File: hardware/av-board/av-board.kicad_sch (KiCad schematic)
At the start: 215 parts, among them J1 RCA Y, J10 2x20 socket, J2 RCA Pb, J3 RCA Pr, J4 RCA L, J5 RCA R, J6 HDMI-001, J9 2x20 socket, SW1 TS-1187A-B-A-B, SW2 TS-1187A-B-A-B, U1 ADV7842KBCZ-5, U10 TPD4E05U06DQAR, U2 ADV7511KSTZ, U3 PCM1808PWR, U4 TLV62569DBVR, U5 TPS7A7001DDAR, U6 TPS7A7001DDAR, U7 TPS7A7001DDAR, U8 TPD4E05U06DQAR, U9 TPD4E05U06DQAR, Y1 28.63636MHz 20pF

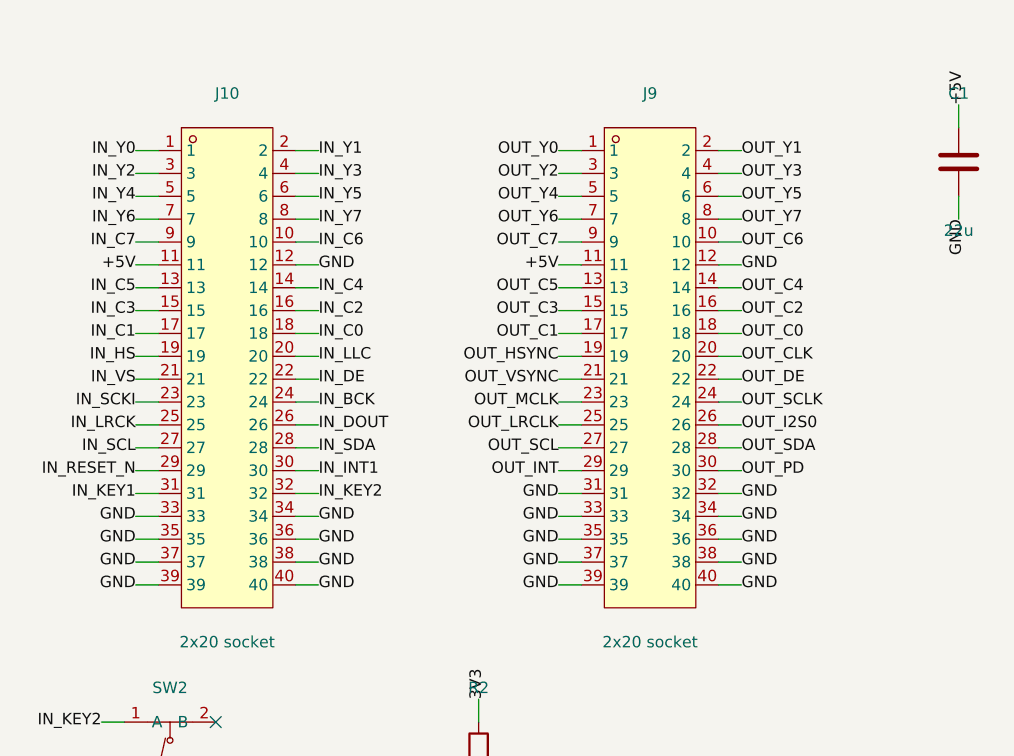
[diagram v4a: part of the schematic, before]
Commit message: Placement: parts by the pins they serve, both header buses flat
The router was failing on placement, not on routing time:

- Small parts were anchored on the first earlier IC sharing any net. Pull-ups to 3V3 went to
  the 3V3 regulator (R20-R25 near J9, 35-45 mm from their ADV7842 balls), and the 51 R
  video terminations (on TERM_x only, no IC pad) fell back to the middle of the bottom edge.
  Now a part on a signal goes to the IC pin it serves, else beside the part it hangs on, else
  the connector pin; supply nets do not count. The terminations sit at the ADV7842 (UG-214
  App. A), the ADV7511 audio series resistors at the source, J9 (HWG 7.3). Parts wait until
  what they hang on is placed.
- J10 had Y0-Y7 on its left pins while the 75 R arrays put out C0..C7 first: every line crossed
  every other in the 5 mm under the arrays. J10 is now in array order (LLC stays on the CLK
  pin: 2 crossings). J9 is in the ADV7511 pin order round the chip (0 crossings); its CLK is
  an output and leaves the header CLK pin. gen_pcb.py prints the crossings per bus.
- The PCM1808 I2S moves from J10 pins 23-26 (45 mm away) to J9 pins 37-40 (10 mm).
- The regulators move out of the band between J9 and the ADV7511 to the empty corner under it.

placecheck.py lists parts far from their nets; snap.py renders a board to PNG. design.md
pin tables follow. ERC clean, schematic = board.py on 897 pins.

Co-Authored-By: Claude Opus 5.5 <noreply@anthropic.com>
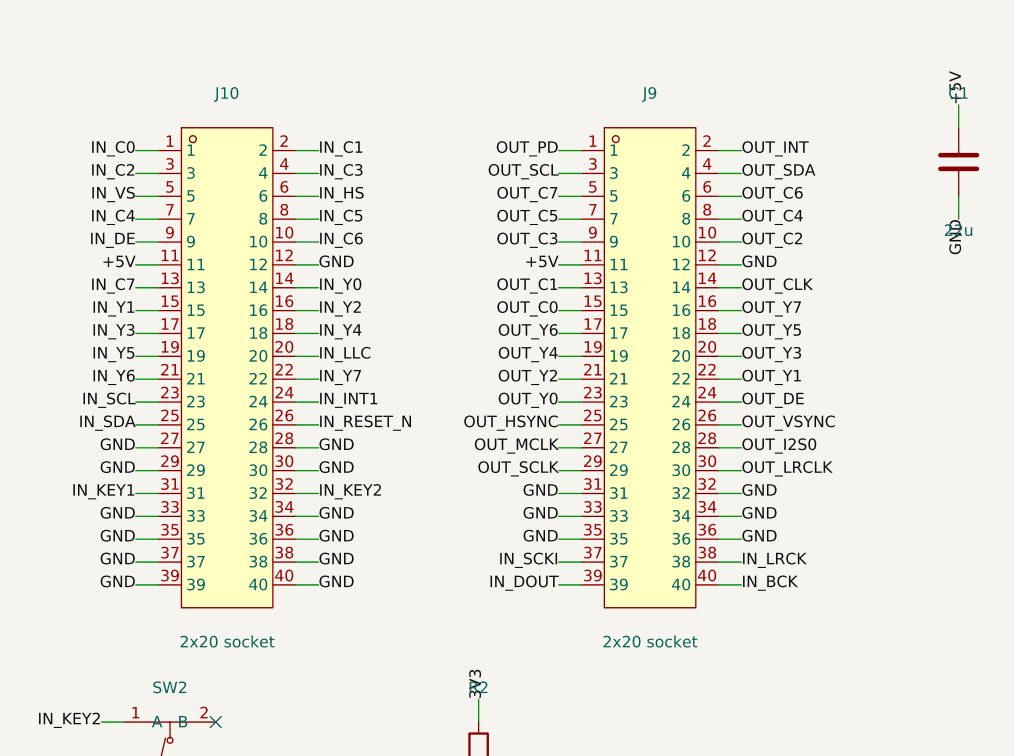
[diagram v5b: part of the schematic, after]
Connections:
- net GND: now also J10.27, J10.28, J10.29, J10.30; no longer J9.37, J9.38, J9.39, J9.40
- net IN_BCK: now also J9.40; no longer J10.24
- net IN_C0: now also J10.1; no longer J10.18
- net IN_C1: now also J10.2; no longer J10.17
- net IN_C2: now also J10.3; no longer J10.16
- net IN_C3: now also J10.4; no longer J10.15
- net IN_C4: now also J10.7; no longer J10.14
- net IN_C5: now also J10.8; no longer J10.13
- net IN_C7: now also J10.13; no longer J10.9
- net IN_DE: now also J10.9; no longer J10.22
- net IN_DOUT: now also J9.39; no longer J10.26
- net IN_HS: now also J10.6; no longer J10.19
- net IN_INT1: now also J10.24; no longer J10.30
- net IN_LRCK: now also J9.38; no longer J10.25
- net IN_RESET_N: now also J10.26; no longer J10.29
- net IN_SCKI: now also J9.37; no longer J10.23
- net IN_SCL: now also J10.23; no longer J10.27
- net IN_SDA: now also J10.25; no longer J10.28
- net IN_VS: now also J10.5; no longer J10.21
- net IN_Y0: now also J10.14; no longer J10.1
- net IN_Y1: now also J10.15; no longer J10.2
- net IN_Y2: now also J10.16; no longer J10.3
- net IN_Y3: now also J10.17; no longer J10.4
- net IN_Y4: now also J10.18; no longer J10.5
- net IN_Y5: now also J10.19; no longer J10.6
- net IN_Y6: now also J10.21; no longer J10.7
- net IN_Y7: now also J10.22; no longer J10.8
- net OUT_C0: now also J9.15; no longer J9.18
- net OUT_C1: now also J9.13; no longer J9.17
- net OUT_C2: now also J9.10; no longer J9.16
- net OUT_C3: now also J9.9; no longer J9.15
- net OUT_C4: now also J9.8; no longer J9.14
- net OUT_C5: now also J9.7; no longer J9.13
- net OUT_C6: now also J9.6; no longer J9.10
- net OUT_C7: now also J9.5; no longer J9.9
- net OUT_CLK: now also J9.14; no longer J9.20
- net OUT_DE: now also J9.24; no longer J9.22
- net OUT_HSYNC: now also J9.25; no longer J9.19
- net OUT_I2S0: now also J9.28; no longer J9.26
- net OUT_INT: now also J9.2; no longer J9.29
- net OUT_LRCLK: now also J9.30; no longer J9.25
- net OUT_MCLK: now also J9.27; no longer J9.23
- net OUT_PD: now also J9.1; no longer J9.30
- net OUT_SCL: now also J9.3; no longer J9.27
- net OUT_SCLK: now also J9.29; no longer J9.24
- net OUT_SDA: now also J9.4; no longer J9.28
- net OUT_VSYNC: now also J9.26; no longer J9.21
- net OUT_Y0: now also J9.23; no longer J9.1
- net OUT_Y1: now also J9.22; no longer J9.2
- net OUT_Y2: now also J9.21; no longer J9.3
- net OUT_Y3: now also J9.20; no longer J9.4
- net OUT_Y4: now also J9.19; no longer J9.5
- net OUT_Y5: now also J9.18; no longer J9.6
- net OUT_Y6: now also J9.17; no longer J9.7
- net OUT_Y7: now also J9.16; no longer J9.8

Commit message: Rail planes sized for their caps: 68 of 69 ADV7842 rail caps over their plane
40 of the ADV7842 rail caps sat off their planes (median 7 mm, up to 12 mm from their rail),
among them 10 per-ball 10/100 nF caps and AVDD/PVDD caps: noise on the ADC and PLL supplies,
and one more routed connection each into the crowd round the BGA.

- The planes widen past the BGA to hold their filter and every cap: AVDD over the top right,
  PVDD over the top left (taking room TVDD did not use), VDD and DVDDIO to the right with
  DVDDIO (25 caps per UG-214 Fig. 179) taking the larger lower part, up to the regulators.
- CVDD's filter and tantalum move from the right of the BGA, where they took VDD/DVDDIO room,
  to its left, four rows from the CVDD balls (C12-E12), in TVDD's spare room.
- The regulators move right, off the planes; U5/U4 spread so the buck has room.
- 10 uF rail caps go by their filter with the 33 uF ones (they are bulk), not round-robin on
  the balls under the BGA's edge.
- Bias resistors (RTERM, R_EXT), the REFP/REFN caps and the regulators' feedback dividers are
  placed before the decoupling, at their pins; the crystal moves 3 mm left, off E15/E16.
- The SDRAM pull-down arrays lose their first-place rank (meant for the 75 R arrays), so the
  analog input caps get the BGA's top edge.
- The PCM1808 VCC ferrite is written down with the PCM1808, so it sits there (was 65 mm away).

PCB=path makes a trial board elsewhere. ERC clean, schematic = board.py (897 pins), DRC: only
the unrouted connections.

Co-Authored-By: Claude Opus 5.5 <noreply@anthropic.com>
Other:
- moved on the sheet: C101, C102, C103, C104, C105, C106, C107, C108, C109, C110, FB1, J4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

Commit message: Review against the data sheets: LDO feed-forward and EN, HPD, anti-alias, clock clearance
Every IC checked pin by pin against its document (design.md "Review against the data sheets"):
the ADV7842 against every row of UG-214 App. C and the AIN_SEL routing, the ADV7511 against
HWG Rev D, the PCM1808, TPS7A7001, TLV62569 and TPD4E05U06 against their data sheets. Fixed:

- TPS7A7001: a 220 pF feed-forward across R1 on all three; the data sheet requires it with
  47-200 uF on the output (3V3 and both 1.8 V rails carry more than 47 uF through the filters).
  U6/U7 output 22 uF -> 10 uF, keeping 1V8A (about 185 uF) under the 200 uF limit.
- TPS7A7001 EN: the 1.8 V LDOs' enable RC now pulls up to 2V5, their VIN; from 3V3 it put EN
  above VIN (recommended: EN <= VIN). The 1.8 V rails still come up about 30 ms after 2V5.
- ADV7511 HPD: 10 k to GND as HWG 6.1.4 asks (was 100 k).
- PCM1808 anti-alias cap 220 pF (145 kHz, TI's range); the 1 nF cut 1.4 dB at 20 kHz.
- A CLOCK netclass (OUT_CLK, LLC) with 0.19 mm clearance, what the 0.5 mm-pitch pads allow
  (HWG 7.2: nothing near the CLK trace).

ERC clean, schematic = board.py (903 pins), DRC: only the unrouted connections.

Co-Authored-By: Claude Opus 5.5 <noreply@anthropic.com>
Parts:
- added C123, C124, C125: 100n, Capacitor_SMD:C_0402_1005Metric, symbol Device:C
- C10: value 10u -> 470n; footprint Capacitor_SMD:C_0805_2012Metric -> Capacitor_SMD:C_0603_1608Metric; LCSC C15850 -> C1623
- C100, C101, C112: value 100n -> 220p; LCSC C1525 -> C1530
- C102: value 10u -> 10n; footprint Capacitor_SMD:C_0603_1608Metric -> Capacitor_SMD:C_0402_1005Metric; LCSC C19702 -> C15195
- C104, C106: value 10u -> 100n; footprint Capacitor_SMD:C_0603_1608Metric -> Capacitor_SMD:C_0402_1005Metric; LCSC C19702 -> C1525
- C105, C29, C30, C31, C40: value 100n -> 10u; footprint Capacitor_SMD:C_0402_1005Metric -> Capacitor_SMD:C_0603_1608Metric; LCSC C1525 -> C19702
- C107, C109: value 1n -> 10u; footprint Capacitor_SMD:C_0402_1005Metric -> Capacitor_SMD:C_0603_1608Metric; LCSC C1523 -> C19702
- C108: value 1u -> 100n; footprint Capacitor_SMD:C_0603_1608Metric -> Capacitor_SMD:C_0402_1005Metric; LCSC C15849 -> C1525
- C11: value 22u -> 10u; LCSC C45783 -> C15850
- C110: value 1u -> 220p; footprint Capacitor_SMD:C_0603_1608Metric -> Capacitor_SMD:C_0402_1005Metric; LCSC C15849 -> C1530
- C111, C113: value 100n -> 1u; footprint Capacitor_SMD:C_0402_1005Metric -> Capacitor_SMD:C_0603_1608Metric; LCSC C1525 -> C15849
- C13: value 22u -> 220p; footprint Capacitor_SMD:C_0805_2012Metric -> Capacitor_SMD:C_0402_1005Metric; LCSC C45783 -> C1530
- C14: value 33u -> 10u; footprint lcsc:CAP-SMD_L3.5-W2.8-R-RD -> Capacitor_SMD:C_0805_2012Metric; symbol lcsc:TAJB336K010RNJ -> Device:C; LCSC C7202 -> C15850
- C15: footprint Capacitor_SMD:C_0603_1608Metric -> Capacitor_SMD:C_0805_2012Metric; LCSC C19702 -> C15850
- C16: value 33u -> 220p; footprint lcsc:CAP-SMD_L3.5-W2.8-R-RD -> Capacitor_SMD:C_0402_1005Metric; symbol lcsc:TAJB336K010RNJ -> Device:C; LCSC C7202 -> C1530
- C17, C19, C21, C23, C25, C27: value 10u -> 33u; footprint Capacitor_SMD:C_0603_1608Metric -> lcsc:CAP-SMD_L3.5-W2.8-R-RD; symbol Device:C -> lcsc:TAJB336K010RNJ; LCSC C19702 -> C7202
- C18, C20, C22, C24: value 33u -> 10u; footprint lcsc:CAP-SMD_L3.5-W2.8-R-RD -> Capacitor_SMD:C_0603_1608Metric; symbol lcsc:TAJB336K010RNJ -> Device:C; LCSC C7202 -> C19702
- C32: value 1n -> 100n; LCSC C1523 -> C1525
- C33, C34: value 30p -> 100n; LCSC C1570 -> C1525
- C35: value 100n -> 1n; LCSC C1525 -> C1523
- C36: value 100n -> 30p; LCSC C1525 -> C1570
- C37: value 10u -> 30p; footprint Capacitor_SMD:C_0603_1608Metric -> Capacitor_SMD:C_0402_1005Metric; LCSC C19702 -> C1570
- C38, C39, C71: value 10n -> 100n; LCSC C15195 -> C1525
- C41, C68: value 100n -> 10n; LCSC C1525 -> C15195
- C42, C56, C57, C58, C74, C75, C86, C87, C88: value 220p -> 10n; LCSC C1530 -> C15195
- C43, C44: value 220p -> 100n; LCSC C1530 -> C1525
- C51, C52, C53, C65, C66, C67, C77, C78, C99: value 10n -> 220p; LCSC C15195 -> C1530
- C6: value 4.7u -> 220p; footprint Capacitor_SMD:C_0805_2012Metric -> Capacitor_SMD:C_0402_1005Metric; LCSC C1779 -> C1530
- C7: value 10u -> 4.7u; LCSC C15850 -> C1779
- C8: value 6.8p -> 10u; footprint Capacitor_SMD:C_0402_1005Metric -> Capacitor_SMD:C_0805_2012Metric; LCSC C1576 -> C15850
- C9: value 470n -> 6.8p; footprint Capacitor_SMD:C_0603_1608Metric -> Capacitor_SMD:C_0402_1005Metric; LCSC C1623 -> C1576
- R51: value 100k -> 10k; LCSC C25741 -> C25744; Note keeps HPD low with no cable (not in HWG Fig. 27) -> 0 V on HPD with no sink [HWG 6.1.4: 10 k +-10 %]
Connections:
- net +5V: now also C7.1; no longer C6.1
- net 1V8A: now also C12.1, C13.1; no longer C11.1
- net 1V8B: now also C15.1, C16.1; no longer C13.1
- net 2V5: now also C11.1, C14.1, C9.1, R7.1; no longer C10.1, C12.1, C7.1
- net 3V3: now also C108.1, C109.1, C6.1, C124.1; no longer C105.1, C106.1, C121.1, R7.1
- net 5VA: now also C106.1, C107.1; no longer C103.1, C104.1
- net AIN_PB: now also C33.2; no longer C30.2
- net AIN_PR: now also C34.2; no longer C31.2
- net AIN_Y: now also C32.2; no longer C29.2
- net AUD_DIV_L: now also C110.1, C111.1; no longer C107.1, C108.1
- net AUD_DIV_R: now also C112.1, C113.1; no longer C109.1, C110.1
- net AUD_VINL: now also C111.2; no longer C108.2
- net AUD_VINR: now also C113.2; no longer C110.2
- net AV_AVDD: now also C19.1, C20.1, C65.1, C66.1, C67.1; no longer C16.1, C17.1, C51.1, C52.1, C53.1
- net AV_CVDD: now also C21.1, C22.1, C69.1, C70.1, C71.1; no longer C18.1, C19.1, C65.1, C66.1, C67.1
- net AV_DVDDIO: now also C100.1, C101.1, C25.1, C26.1, C99.1; no longer C22.1, C23.1, C76.1, C77.1, C78.1
- net AV_PVDD: now also C102.1, C103.1, C23.1, C24.1; no longer C100.1, C20.1, C21.1, C99.1
- net AV_TVDD: now also C27.1, C28.1, C51.1, C52.1, C53.1; no longer C24.1, C25.1, C38.1, C39.1, C40.1
- net AV_VDD: now also C17.1, C18.1, C76.1, C77.1, C78.1; no longer C14.1, C15.1, C69.1, C70.1, C71.1
- net EN_1V8: now also C10.1; no longer C9.1
- net FB_1V8A: now also C13.2
- net FB_1V8B: now also C16.2
- net FB_2V5: now also C9.2; no longer C8.2
- net FB_3V3: now also C6.2
- net GND: now also C108.2, C110.2, C29.2, C30.2, C31.2, C37.2, C8.2, C123.2, C124.2, C125.2; no longer C111.2, C113.2, C13.2, C16.2, C33.2, C34.2, C35.2, C40.2, C6.2, C9.2
- net HDMI_5V: now also C125.1; no longer C122.1
- net REFN: now also C39.1, C40.2; no longer C36.1, C37.2
- net REFP: now also C38.1, C40.1; no longer C35.1, C37.1
- net SYNC_Y: now also C35.2; no longer C32.2
- net TERM_PB: now also C33.1; no longer C30.1
- net TERM_PR: now also C34.1; no longer C31.1
- net TERM_Y: now also C35.1; no longer C29.1
- net TX_AVDD: now also C119.1, C120.1, C121.1, C30.1; no longer C115.1, C116.1, C117.1, C27.1
- net TX_DVDD: now also C115.1, C116.1, C117.1, C29.1; no longer C111.1, C112.1, C113.1, C26.1
- net TX_PLVDD: now also C122.1, C31.1, C123.1; no longer C119.1, C120.1, C28.1
- net VREF: now also C104.1, C105.1; no longer C101.1, C102.1
- net XTALN: now also C37.1; no longer C34.1
- net XTALP: now also C36.1; no longer C33.1
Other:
- moved on the sheet: C10, C100, C101, C102, C103, C104, C105, C106, C107, C108, C109, C11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

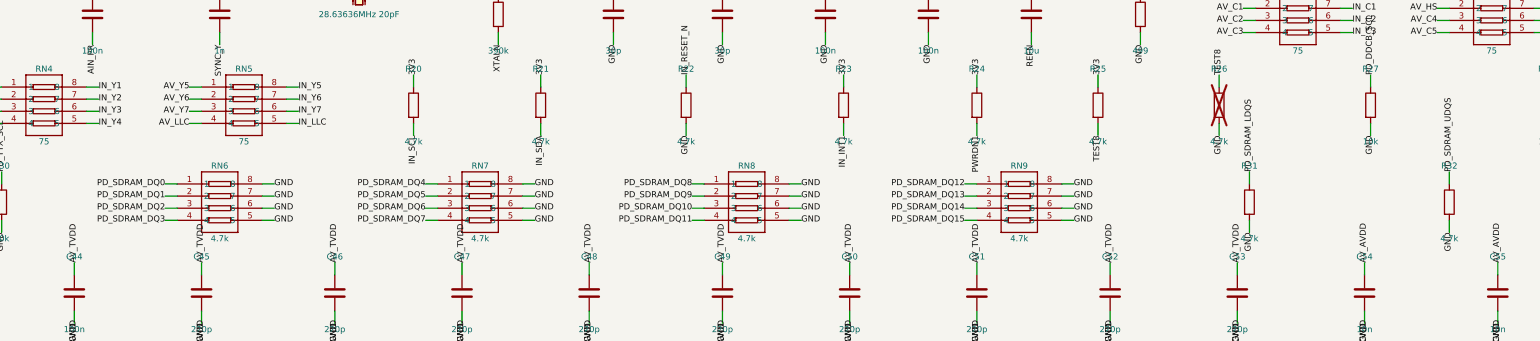
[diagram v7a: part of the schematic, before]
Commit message: SDRAM pull-downs grouped by ball position, arrays along the BGA's right side; six layers default
The pull-down arrays were grouped by DQ number, so each collected four lines from scattered
balls across the BGA's top right corner (RN8: R16, R15, T15 and N14, four rows in), and lines
for different arrays crossed in the tightest spot on the board. Any pin may take any of these
identical 4.7 k pull-downs, so:

- board.py orders the 18 balls along the chip's T-row edge (column, then row); each array serves
  four neighbouring balls, the two at the ends of the run take single resistors.
- gen_pcb.py's array placer (was place_rn, for the 75 R arrays) takes any side: the pull-down
  arrays now stand in a column down the ADV7842's right side, each level with its balls, pads
  towards the chip in ball order.
- Six layers are the default (LAYERS=4 does not route); design.md says why, with the results.

ERC clean, schematic = board.py (903 pins), DRC: only the unrouted connections.

Co-Authored-By: Claude Opus 5.5 <noreply@anthropic.com>
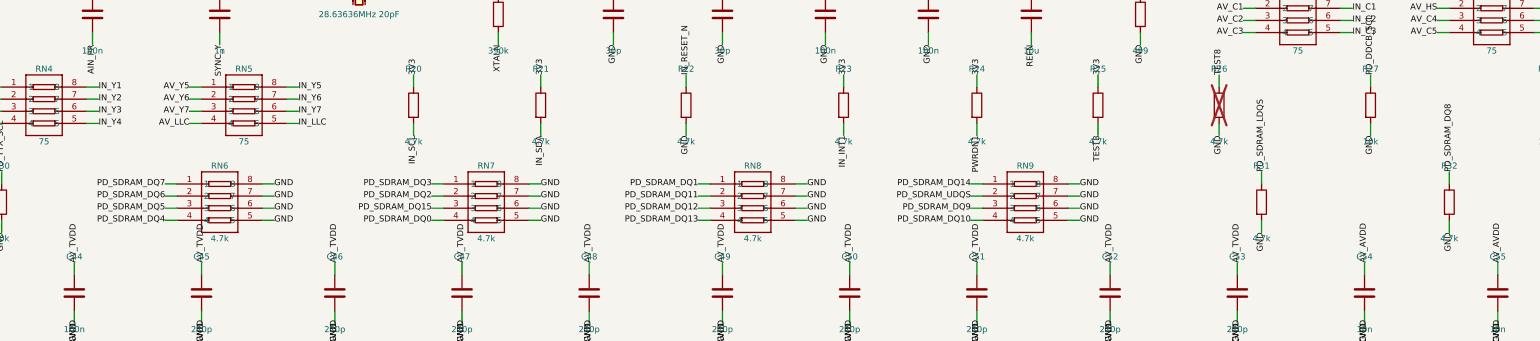
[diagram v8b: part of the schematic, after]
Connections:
- net PD_SDRAM_DQ0: now also RN7.4; no longer RN6.1
- net PD_SDRAM_DQ1: now also RN8.1; no longer RN6.2
- net PD_SDRAM_DQ10: now also RN9.4; no longer RN8.3
- net PD_SDRAM_DQ11: now also RN8.2; no longer RN8.4
- net PD_SDRAM_DQ12: now also RN8.3; no longer RN9.1
- net PD_SDRAM_DQ13: now also RN8.4; no longer RN9.2
- net PD_SDRAM_DQ14: now also RN9.1; no longer RN9.3
- net PD_SDRAM_DQ15: now also RN7.3; no longer RN9.4
- net PD_SDRAM_DQ2: now also RN7.2; no longer RN6.3
- net PD_SDRAM_DQ3: now also RN7.1; no longer RN6.4
- net PD_SDRAM_DQ4: now also RN6.4; no longer RN7.1
- net PD_SDRAM_DQ5: now also RN6.3; no longer RN7.2
- net PD_SDRAM_DQ6: now also RN6.2; no longer RN7.3
- net PD_SDRAM_DQ7: now also RN6.1; no longer RN7.4
- net PD_SDRAM_DQ8: now also R32.1; no longer RN8.1
- net PD_SDRAM_DQ9: now also RN9.3; no longer RN8.2
- net PD_SDRAM_UDQS: now also RN9.2; no longer R32.1
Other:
- moved on the sheet: R31, RN7, RN8, RN9
